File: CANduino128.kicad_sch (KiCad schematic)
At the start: 63 parts, among them J1 Conn_02x32_Row_Letter_First, J2 Conn_01x10, U1 AVR-H128-CAN, U2 74AHC373

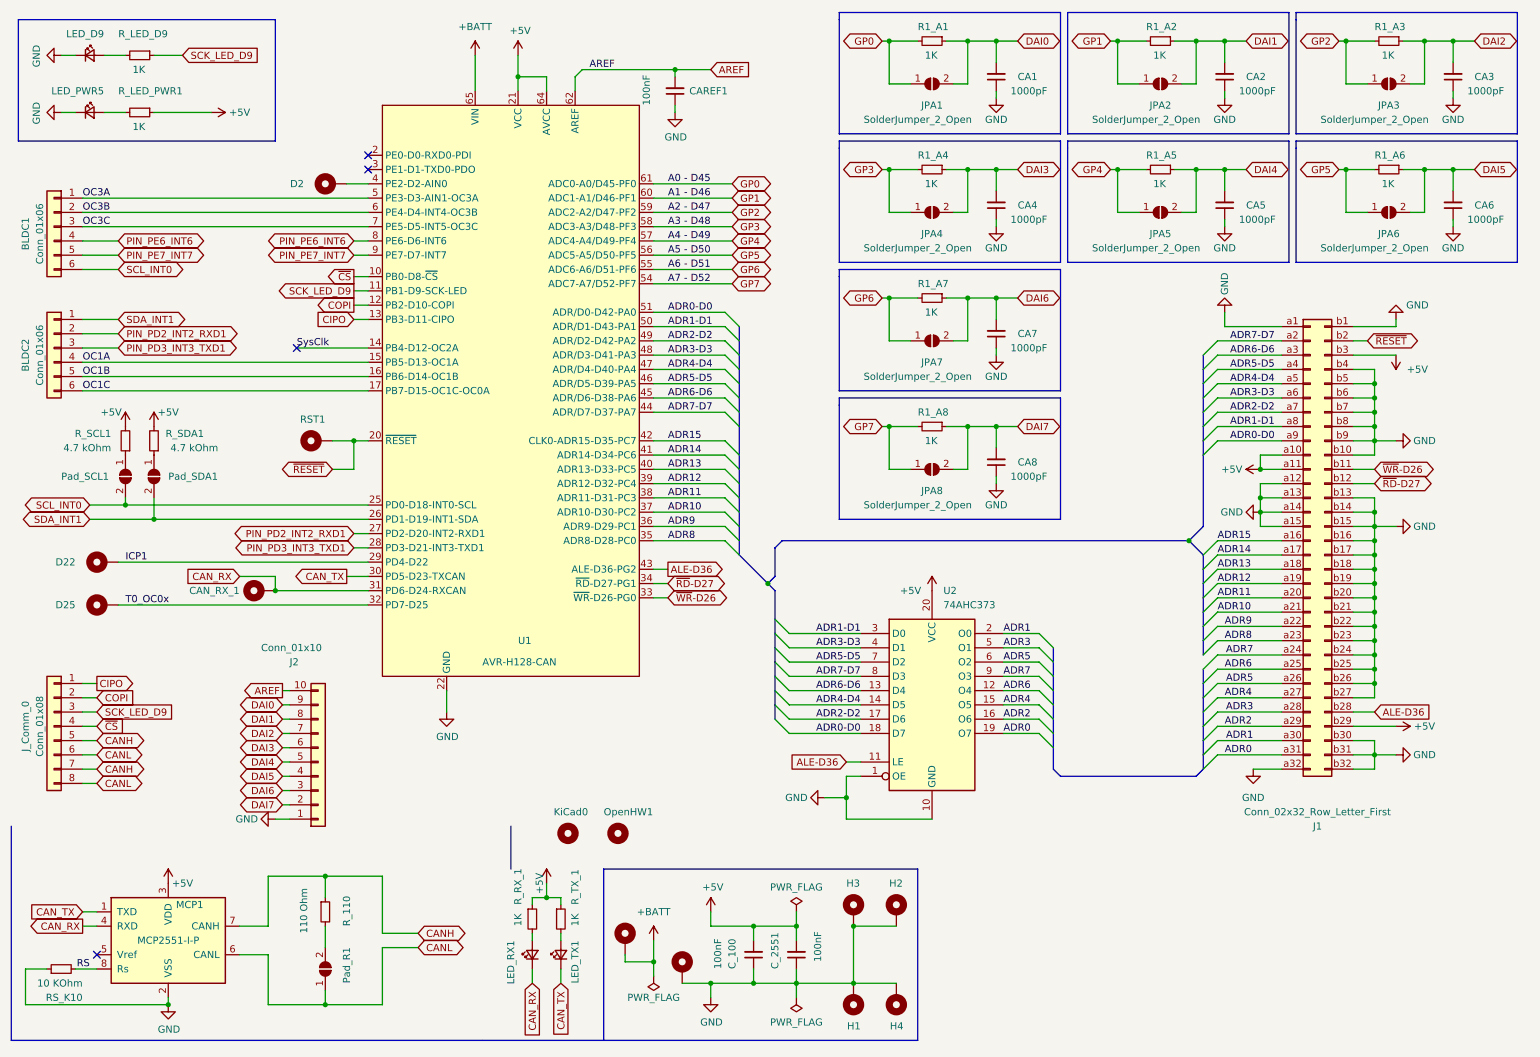
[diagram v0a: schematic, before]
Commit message: A envoyer en prod. - câblage Reset (avec "via") - câblage T0_0C0x - câblage ICP1 - correction silskreen
git-svn-id: file:///D%5C00%20-%20Dev%20&%20Calculs%5CRepoTortoiseSVN_PCB%5CCANduino128/branches/CANduino128%20-%20v3.0a@43 67ddf66f-3787-a644-8df7-7746e21a92b3
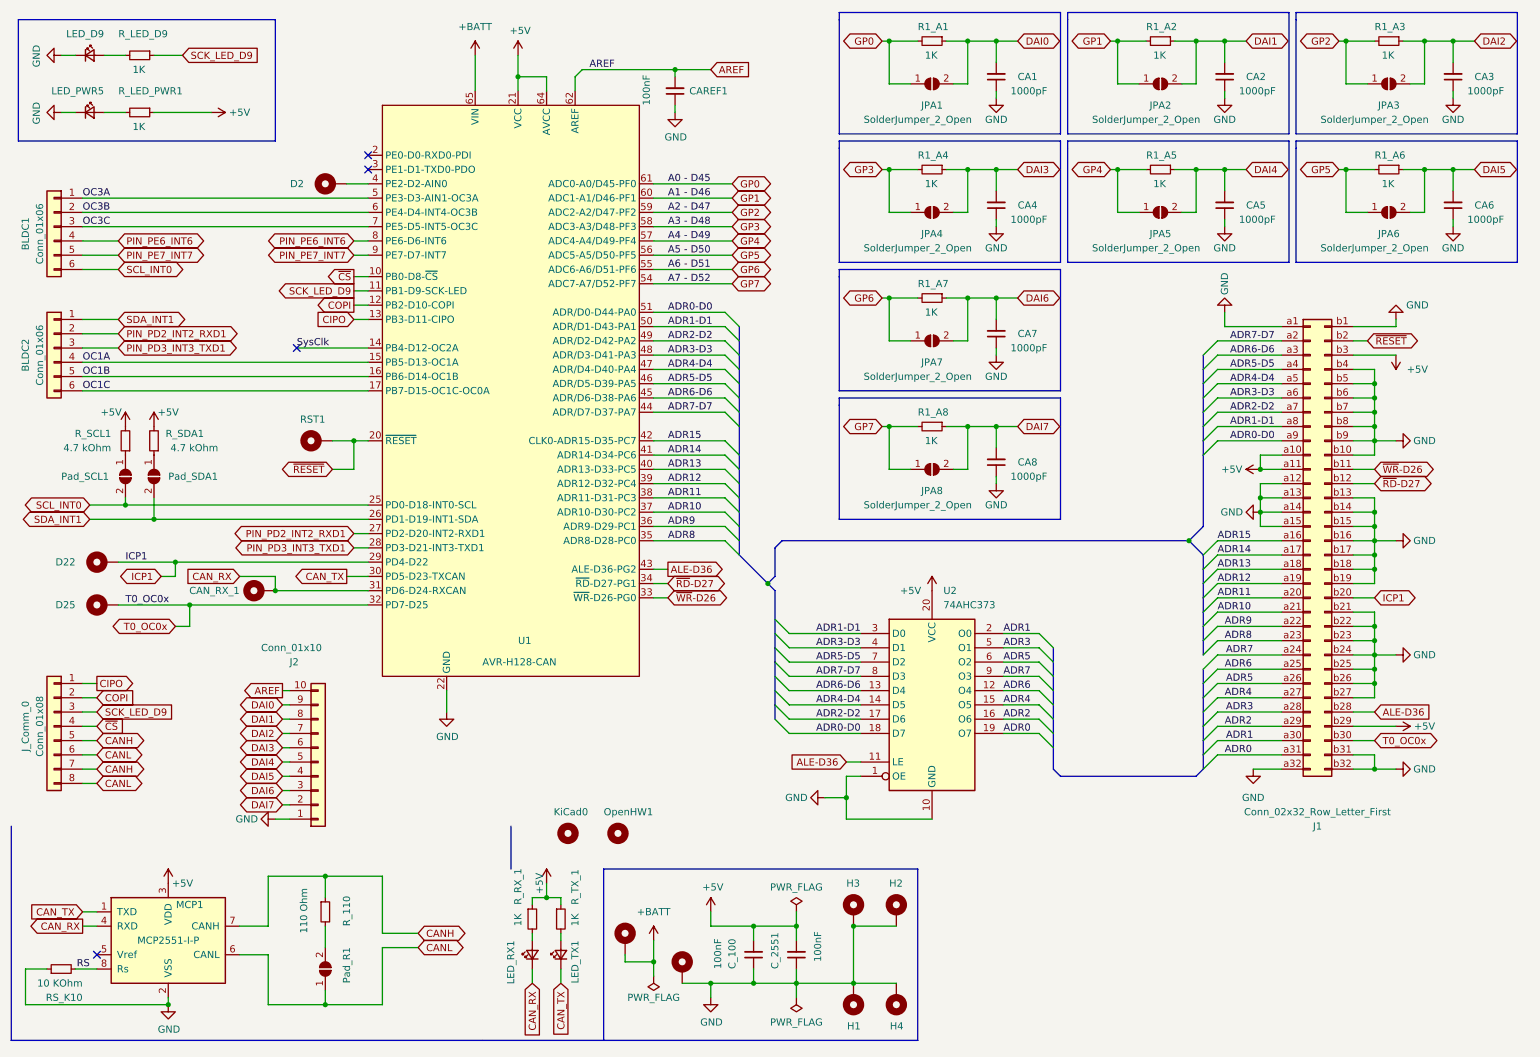
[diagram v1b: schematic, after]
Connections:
- net GND: no longer J1.b20 (Pin_b20), J1.b30 (Pin_b30)
- net ICP1: now also J1.b20 (Pin_b20)
- net T0_OC0x: now also J1.b30 (Pin_b30)

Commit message: - Carry-over de la correction sur inversion des bornes d'entrées/sorties des circuits des pins analogiques. - Correction de plusieurs valeurs électriques sur le port ISA8 des pins non utilisées - Reste à éclaircir la légitimité de ce qu'il y a été fait sur les pins ALE, BALE et AEN. (fonctionnement probablement incompatible avec le standard ISA8)
- Préparation marquage v3.1
- Génération des fichiers de fabrication par principe

git-svn-id: file:///D%5C00%20-%20Dev%20&%20Calculs%5CRepoTortoiseSVN_PCB%5CCANduino128/tags/CANduino128%20-%20v3.0@68 67ddf66f-3787-a644-8df7-7746e21a92b3
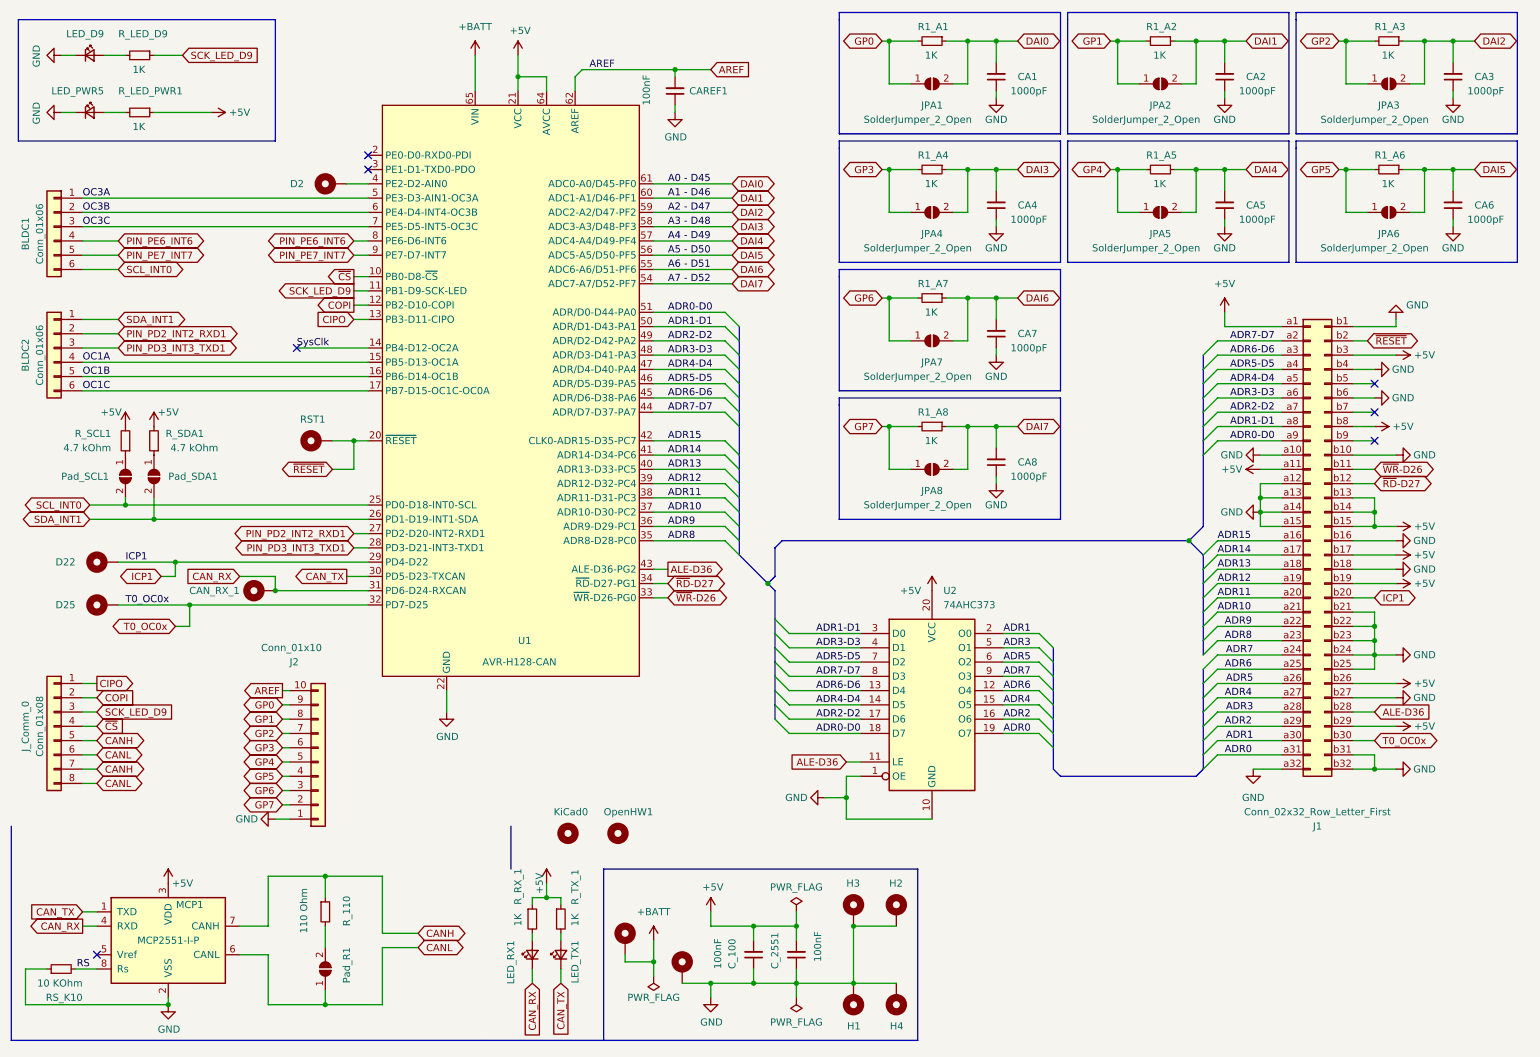
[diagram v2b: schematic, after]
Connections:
- net +5V: now also J1.a1 (Pin_a1), J1.b13 (Pin_b13), J1.b14 (Pin_b14), J1.b15 (Pin_b15), J1.b17 (Pin_b17), J1.b19 (Pin_b19), J1.b26 (Pin_b26), J1.b8 (Pin_b8); no longer J1.a10 (Pin_a10)
- net DAI0: now also U1.61 (ADC0-A0/D45-PF0); no longer J2.9 (Pin_9)
- net DAI1: now also U1.60 (ADC1-A1/D46-PF1); no longer J2.8 (Pin_8)
- net DAI2: now also U1.59 (ADC2-A2/D47-PF2); no longer J2.7 (Pin_7)
- net DAI3: now also U1.58 (ADC3-A3/D48-PF3); no longer J2.6 (Pin_6)
- net DAI4: now also U1.57 (ADC4-A4/D49-PF4); no longer J2.5 (Pin_5)
- net DAI5: now also U1.56 (ADC5-A5/D50-PF5); no longer J2.4 (Pin_4)
- net DAI6: now also U1.55 (ADC6-A6/D51-PF6); no longer J2.3 (Pin_3)
- net DAI7: now also U1.54 (ADC7-A7/D52-PF7); no longer J2.2 (Pin_2)
- net GND: now also J1.a10 (Pin_a10); no longer J1.a1 (Pin_a1), J1.b13 (Pin_b13), J1.b14 (Pin_b14), J1.b15 (Pin_b15), J1.b17 (Pin_b17), J1.b19 (Pin_b19), J1.b26 (Pin_b26), J1.b5 (Pin_b5), J1.b7 (Pin_b7), J1.b8 (Pin_b8), J1.b9 (Pin_b9)
- net GP0: now also J2.9 (Pin_9); no longer U1.61 (ADC0-A0/D45-PF0)
- net GP1: now also J2.8 (Pin_8); no longer U1.60 (ADC1-A1/D46-PF1)
- net GP2: now also J2.7 (Pin_7); no longer U1.59 (ADC2-A2/D47-PF2)
- net GP3: now also J2.6 (Pin_6); no longer U1.58 (ADC3-A3/D48-PF3)
- net GP4: now also J2.5 (Pin_5); no longer U1.57 (ADC4-A4/D49-PF4)
- net GP5: now also J2.4 (Pin_4); no longer U1.56 (ADC5-A5/D50-PF5)
- net GP6: now also J2.3 (Pin_3); no longer U1.55 (ADC6-A6/D51-PF6)
- net GP7: now also J2.2 (Pin_2); no longer U1.54 (ADC7-A7/D52-PF7)
- no-connect marks 4 -> 7

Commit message: On carréïse le form-factor avec des angles à 1.2mm de rayon On branche le +Batt sur la port ISA en lieu et place du +12V On arrange le silkscreen du port ISA pour tenir compte des +5V et des GND de base hors stubb
git-svn-id: file:///D%5C00%20-%20Dev%20&%20Calculs%5CRepoTortoiseSVN_PCB%5CCANduino128/tags/CANduino128%20-%20v3.0@69 67ddf66f-3787-a644-8df7-7746e21a92b3
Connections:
- net +BATT: now also J1.b9 (Pin_b9)
- no-connect marks 7 -> 6
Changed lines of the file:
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@@
   (no_connect (at 77.47 41.91))
   (no_connect (at 64.77 73.66))
-  (no_connect (at 256.54 90.17))
   (bus_entry (at 228.6 77.47) (size -2.54 2.54)
     (stroke (width 0) (type default) (color 0 0 0 0))
@@
     (stroke (width 0) (type default) (color 0 0 0 0))
   )
-  (polyline (pts (xy 102.87 166.37) (xy 102.87 158.75))
-    (stroke (width 0) (type default) (color 0 0 0 0))
-  )
   (polyline (pts (xy 281.94 13.97) (xy 242.57 13.97))
     (stroke (width 0) (type default) (color 0 0 0 0))
@@
     (stroke (width 0) (type default) (color 0 0 0 0))
   )
+  (polyline (pts (xy 119.38 163.83) (xy 119.38 166.37))
+    (stroke (width 0) (type default) (color 0 0 0 0))
+  )
   (wire (pts (xy 59.69 190.5) (xy 69.85 190.5))
     (stroke (width 0) (type default) (color 0 0 0 0))
@@
     (stroke (width 0) (type default) (color 0 0 0 0))
   )
+  (polyline (pts (xy 109.22 163.83) (xy 119.38 163.83))
+    (stroke (width 0) (type default) (color 0 0 0 0))
+  )
   (wire (pts (xy 233.68 41.91) (xy 229.87 41.91))
     (stroke (width 0) (type default) (color 0 0 0 0))
@@
     (stroke (width 0) (type default) (color 0 0 0 0))
   )
+  (polyline (pts (xy 13.97 158.75) (xy 50.8 158.75))
+    (stroke (width 0) (type default) (color 0 0 0 0))
+  )
   (wire (pts (xy 256.54 146.05) (xy 256.54 148.59))
     (stroke (width 0) (type default) (color 0 0 0 0))
@@
     (stroke (width 0) (type default) (color 0 0 0 0))
   )
+  (polyline (pts (xy 50.8 158.75) (xy 50.8 161.29))
+    (stroke (width 0) (type default) (color 0 0 0 0))
+  )
   (wire (pts (xy 62.23 139.7) (xy 63.5 139.7))
     (stroke (width 0) (type default) (color 0 0 0 0))
@@
     (stroke (width 0) (type default) (color 0 0 0 0))
   )
+  (polyline (pts (xy 50.8 161.29) (xy 109.22 161.29))
+    (stroke (width 0) (type default) (color 0 0 0 0))
+  )
   (polyline (pts (xy 242.57 36.83) (xy 242.57 38.1))
     (stroke (width 0) (type default) (color 0 0 0 0))
@@
     (stroke (width 0) (type default) (color 0 0 0 0))
   )
+  (polyline (pts (xy 109.22 161.29) (xy 109.22 163.83))
+    (stroke (width 0) (type default) (color 0 0 0 0))
+  )
   (wire (pts (xy 224.79 41.91) (xy 224.79 49.53))
     (stroke (width 0) (type default) (color 0 0 0 0))
@@
     (pin "1")
   )
+  (symbol (lib_id "power:+BATT") (at 256.54 90.17 270) (unit 1)
+    (in_bom yes) (on_board yes) (fields_autoplaced)
+    (property "Reference" "#PWR?" (id 0) (at 252.73 90.17 0)
+      (effects (font (size 1.27 1.27)) hide)
+    )
+    (property "Value" "+BATT" (id 1) (at 260.35 90.1699 90)
+      (effects (font (size 1.27 1.27)) (justify left))
+    )
+    (property "Footprint" "" (id 2) (at 256.54 90.17 0)
+      (effects (font (size 1.27 1.27)) hide)
+    )
+    (property "Datasheet" "" (id 3) (at 256.54 90.17 0)
+      (effects (font (size 1.27 1.27)) hide)
+    )
+    (pin "1")
+  )
   (symbol (lib_id "power:GND") (at 22.86 31.75 270) (unit 1)
     (in_bom yes) (on_board yes)
@@
       (reference "#PWR0147") (unit 1) (value "+5V") (footprint "")
     )
+    (path "/79aedb82-5897-478d-abbc-4679fbc14d36"
+      (reference "#PWR?") (unit 1) (value "+BATT") (footprint "")
+    )
     (path "/98d06520-137f-4783-b6e5-5a12e7210f91"
